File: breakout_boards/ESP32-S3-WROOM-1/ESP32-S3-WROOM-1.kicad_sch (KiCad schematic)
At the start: 47 parts, among them J1 USB_C_Receptacle_USB2.0_16P, J2 JST-XH 6 pin, J4 JST-XH 6 pin, SW1 SW_Push, SW2 SW_Push, U1 ESP32-S3-WROOM-1, U2 AP7361-33E

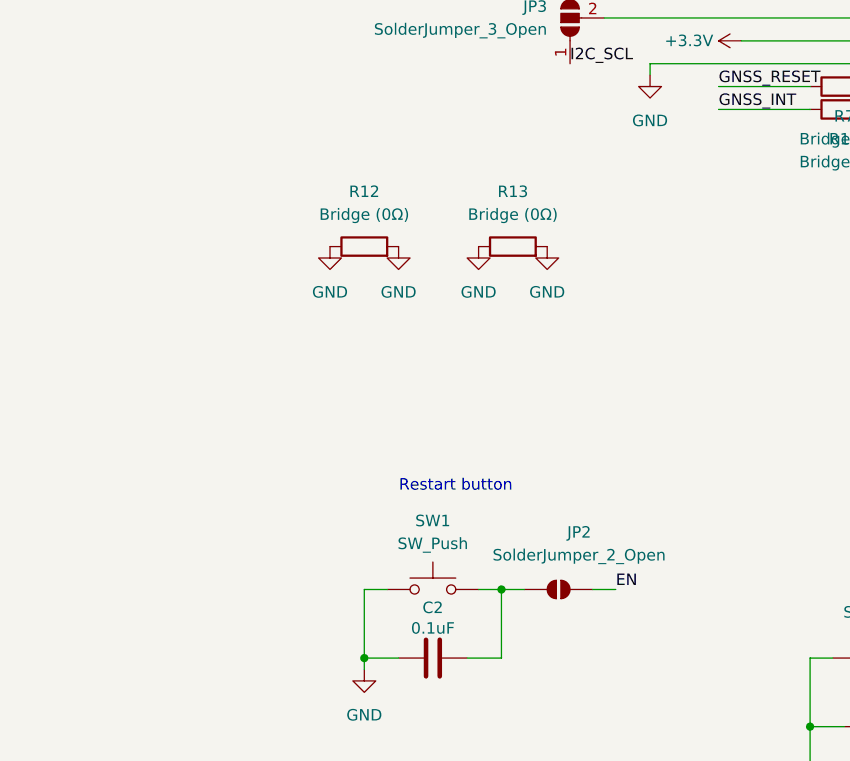
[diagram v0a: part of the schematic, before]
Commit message: Fixed ESP32-WROOM breakout board
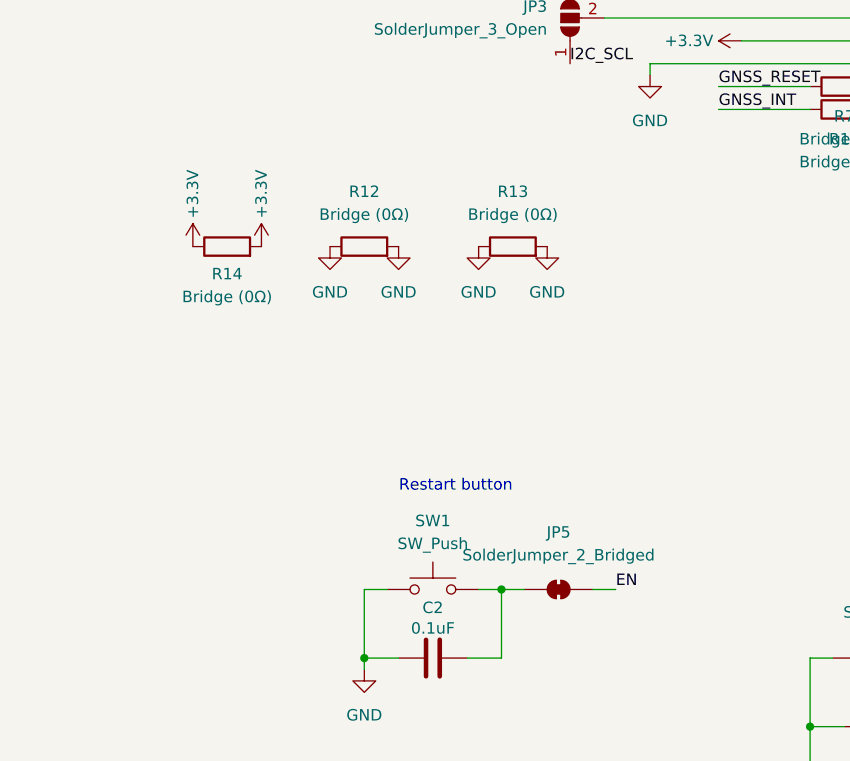
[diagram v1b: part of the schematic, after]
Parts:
- removed JP2: SolderJumper_2_Open, Jumper:SolderJumper-2_P1.3mm_Open_RoundedPad1.0x1.5mm, symbol Jumper:SolderJumper_2_Open
- added JP5: SolderJumper_2_Bridged, Jumper:SolderJumper-2_P1.3mm_Bridged_RoundedPad1.0x1.5mm, symbol Jumper:SolderJumper_2_Bridged
- added R14: Bridge (0Ω), Resistor_THT:R_Axial_DIN0207_L6.3mm_D2.5mm_P10.16mm_Horizontal, symbol Device:R
- R10: footprint Resistor_THT:R_Axial_DIN0204_L3.6mm_D1.6mm_P5.08mm_Horizontal -> Resistor_SMD:R_0603_1608Metric_Pad0.98x0.95mm_HandSolder
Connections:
- net +3.3V: now also R14.1, R14.2
- net EN: now also JP5.2 (B)
- net at C2.1, SW1.2: now also JP5.1 (A)
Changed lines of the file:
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@@
 	)
 	(symbol
+		(lib_id "Device:R")
+		(at 184.15 97.79 90)
+		(unit 1)
+		(exclude_from_sim no)
+		(in_bom yes)
+		(on_board yes)
+		(dnp no)
+		(property "Reference" "R14"
+			(at 184.15 100.838 90)
+			(effects
+				(font
+					(size 1.27 1.27)
+				)
+			)
+		)
+		(property "Value" "Bridge (0Ω)"
+			(at 184.15 103.378 90)
+			(effects
+				(font
+					(size 1.27 1.27)
+				)
+			)
+		)
+		(property "Footprint" "Resistor_THT:R_Axial_DIN0207_L6.3mm_D2.5mm_P10.16mm_Horizontal"
+			(at 184.15 99.568 90)
+			(effects
+				(font
+					(size 1.27 1.27)
+				)
+				(hide yes)
+			)
+		)
+		(property "Datasheet" "~"
+			(at 184.15 97.79 0)
+			(effects
+				(font
+					(size 1.27 1.27)
+				)
+				(hide yes)
+			)
+		)
+		(property "Description" "Resistor"
+			(at 184.15 97.79 0)
+			(effects
+				(font
+					(size 1.27 1.27)
+				)
+				(hide yes)
+			)
+		)
+		(pin "1"
+		)
+		(pin "2"
+		)
+		(instances
+			(project "ESP32-S3-WROOM-1"
+				(path "/4c0d9a6e-1f0c-494d-a3d3-03d736fc4cea"
+					(reference "R14")
+					(unit 1)
+				)
+			)
+		)
+	)
+	(symbol
 		(lib_id "Device:C")
 		(at 207.01 143.51 270)
@@
 	)
 	(symbol
+		(lib_id "power:+3.3V")
+		(at 187.96 97.79 0)
+		(unit 1)
+		(exclude_from_sim no)
+		(in_bom yes)
+		(on_board yes)
+		(dnp no)
+		(property "Reference" "#PWR035"
+			(at 187.96 101.6 0)
+			(effects
+				(font
+					(size 1.27 1.27)
+				)
+				(hide yes)
+			)
+		)
+		(property "Value" "+3.3V"
+			(at 187.96 91.948 90)
+			(effects
+				(font
+					(size 1.27 1.27)
+				)
+			)
+		)
+		(property "Footprint" ""
+			(at 187.96 97.79 0)
+			(effects
+				(font
+					(size 1.27 1.27)
+				)
+				(hide yes)
+			)
+		)
+		(property "Datasheet" ""
+			(at 187.96 97.79 0)
+			(effects
+				(font
+					(size 1.27 1.27)
+				)
+				(hide yes)
+			)
+		)
+		(property "Description" "Power symbol creates a global label with name \"+3.3V\""
+			(at 187.96 97.79 0)
+			(effects
+				(font
+					(size 1.27 1.27)
+				)
+				(hide yes)
+			)
+		)
+		(pin "1"
+		)
+		(instances
+			(project "ESP32-S3-WROOM-1"
+				(path "/4c0d9a6e-1f0c-494d-a3d3-03d736fc4cea"
+					(reference "#PWR035")
+					(unit 1)
+				)
+			)
+		)
+	)
+	(symbol
 		(lib_id "Switch:SW_Push")
 		(at 256.54 143.51 0)
@@
 	)
 	(symbol
-		(lib_id "Jumper:SolderJumper_2_Open")
-		(at 220.98 135.89 180)
-		(unit 1)
-		(exclude_from_sim no)
-		(in_bom no)
-		(on_board yes)
-		(dnp no)
-		(property "Reference" "JP2"
-			(at 223.266 129.54 0)
-			(effects
-				(font
-					(size 1.27 1.27)
-				)
-			)
-		)
-		(property "Value" "SolderJumper_2_Open"
-			(at 223.266 132.08 0)
-			(effects
-				(font
-					(size 1.27 1.27)
-				)
-			)
-		)
-		(property "Footprint" "Jumper:SolderJumper-2_P1.3mm_Open_RoundedPad1.0x1.5mm"
-			(at 220.98 135.89 0)
-			(effects
-				(font
-					(size 1.27 1.27)
-				)
-				(hide yes)
-			)
-		)
-		(property "Datasheet" "~"
-			(at 220.98 135.89 0)
-			(effects
-				(font
-					(size 1.27 1.27)
-				)
-				(hide yes)
-			)
-		)
-		(property "Description" "Solder Jumper, 2-pole, open"
-			(at 220.98 135.89 0)
-			(effects
-				(font
-					(size 1.27 1.27)
-				)
-				(hide yes)
-			)
-		)
-		(pin "1"
-		)
-		(pin "2"
-		)
-		(instances
-			(project "ESP32-S3-WROOM-1"
-				(path "/4c0d9a6e-1f0c-494d-a3d3-03d736fc4cea"
-					(reference "JP2")
-					(unit 1)
-				)
-			)
-		)
-	)
-	(symbol
 		(lib_id "Device:C")
 		(at 78.74 59.69 0)
@@
 			)
 		)
-		(property "Footprint" "Resistor_THT:R_Axial_DIN0204_L3.6mm_D1.6mm_P5.08mm_Horizontal"
+		(property "Footprint" "Resistor_SMD:R_0603_1608Metric_Pad0.98x0.95mm_HandSolder"
 			(at 263.652 137.16 90)
 			(effects
@@
 	)
 	(symbol
+		(lib_id "power:+3.3V")
+		(at 180.34 97.79 0)
+		(unit 1)
+		(exclude_from_sim no)
+		(in_bom yes)
+		(on_board yes)
+		(dnp no)
+		(property "Reference" "#PWR033"
+			(at 180.34 101.6 0)
+			(effects
+				(font
+					(size 1.27 1.27)
+				)
+				(hide yes)
+			)
+		)
+		(property "Value" "+3.3V"
+			(at 180.34 91.948 90)
+			(effects
+				(font
+					(size 1.27 1.27)
+				)
+			)
+		)
+		(property "Footprint" ""
+			(at 180.34 97.79 0)
+			(effects
+				(font
+					(size 1.27 1.27)
+				)
+				(hide yes)
+			)
+		)
+		(property "Datasheet" ""
+			(at 180.34 97.79 0)
+			(effects
+				(font
+					(size 1.27 1.27)
+				)
+				(hide yes)
+			)
+		)
+		(property "Description" "Power symbol creates a global label with name \"+3.3V\""
+			(at 180.34 97.79 0)
+			(effects
+				(font
+					(size 1.27 1.27)
+				)
+				(hide yes)
+			)
+		)
+		(pin "1"
+		)
+		(instances
+			(project "ESP32-S3-WROOM-1"
+				(path "/4c0d9a6e-1f0c-494d-a3d3-03d736fc4cea"
+					(reference "#PWR033")
+					(unit 1)
+				)
+			)
+		)
+	)
+	(symbol
 		(lib_id "Connector_Generic:Conn_01x06")
 		(at 261.62 38.1 0)
@@
 					(unit 1)
 				)
+			)
+		)
+	)
+	(symbol
+		(lib_id "Jumper:SolderJumper_2_Bridged")
+		(at 220.98 135.89 0)
+		(unit 1)
+		(exclude_from_sim no)
+		(in_bom no)
+		(on_board yes)
+		(dnp no)
+		(fields_autoplaced yes)
+		(property "Reference" "JP5"
+			(at 220.98 129.54 0)
+			(effects
+				(font
+					(size 1.27 1.27)
+				)
+			)
+		)
+		(property "Value" "SolderJumper_2_Bridged"
+			(at 220.98 132.08 0)
+			(effects
+				(font
+					(size 1.27 1.27)
+				)
+			)
+		)
+		(property "Footprint" "Jumper:SolderJumper-2_P1.3mm_Bridged_RoundedPad1.0x1.5mm"
+			(at 220.98 135.89 0)
+			(effects
+				(font
+					(size 1.27 1.27)
+				)
+				(hide yes)
+			)
+		)
+		(property "Datasheet" "~"
+			(at 220.98 135.89 0)
+			(effects
+				(font
+					(size 1.27 1.27)
+				)
+				(hide yes)
+			)
+		)
+		(property "Description" "Solder Jumper, 2-pole, closed/bridged"
+			(at 220.98 135.89 0)
+			(effects
+				(font
+					(size 1.27 1.27)
+				)
+				(hide yes)
+			)
+		)
+		(pin "2"
+		)
+		(pin "1"
+		)
+		(instances
+			(project ""
+				(path "/4c0d9a6e-1f0c-494d-a3d3-03d736fc4cea"
+					(reference "JP5")
+					(unit 1)
+				)

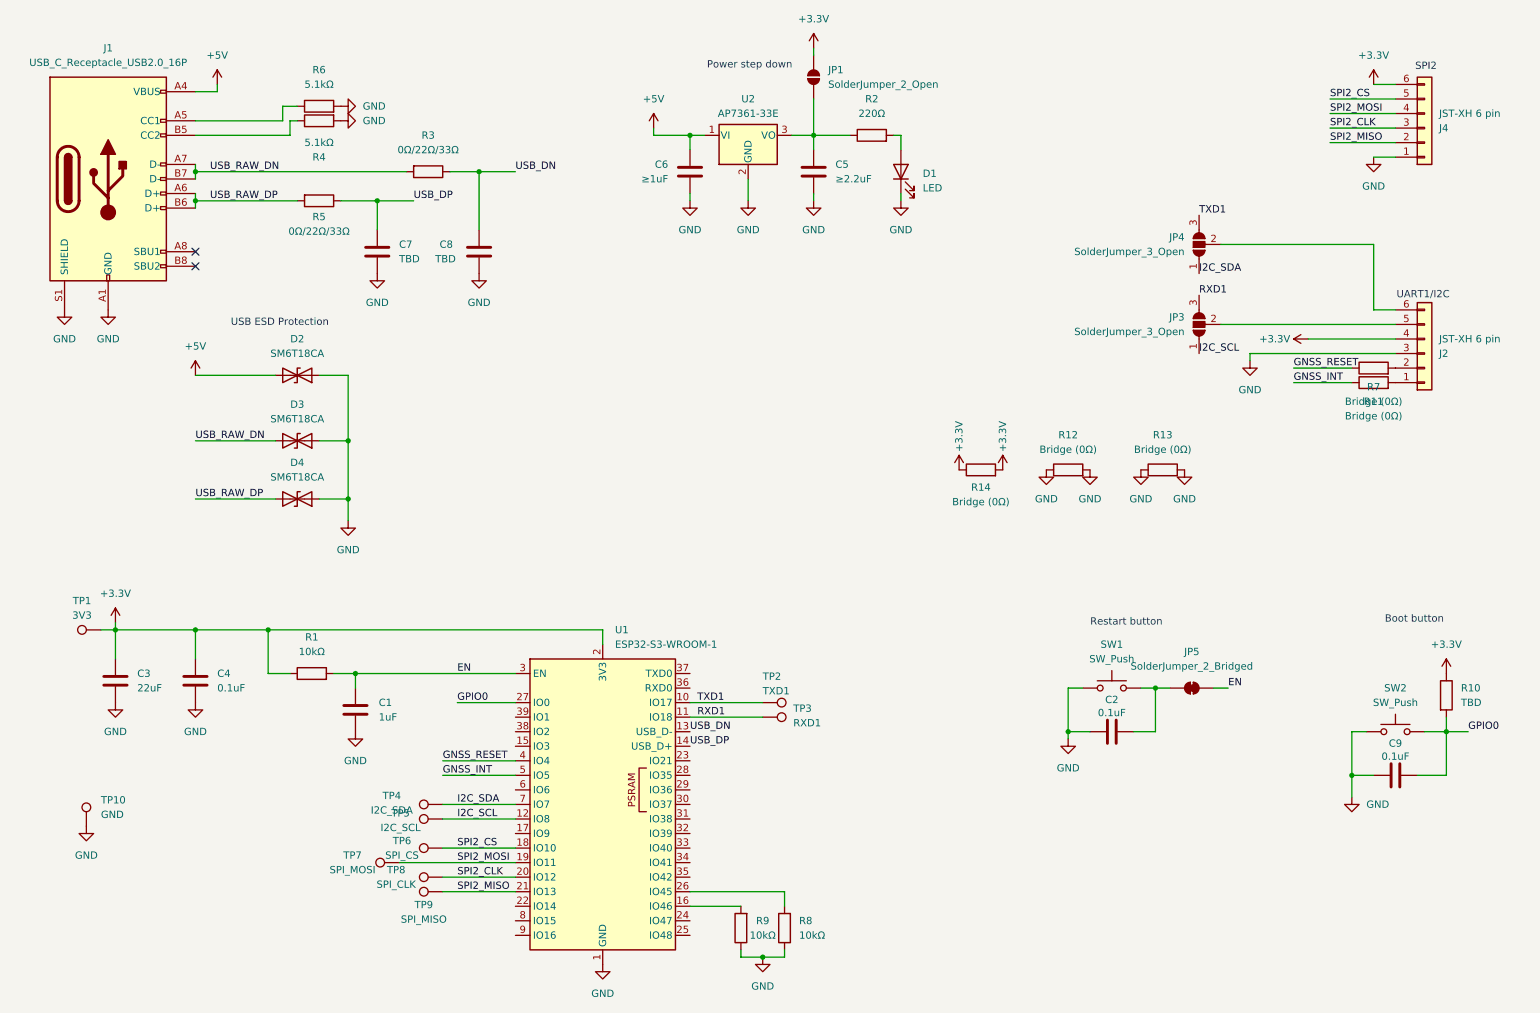
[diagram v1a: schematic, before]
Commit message: edited values to match real life and added text
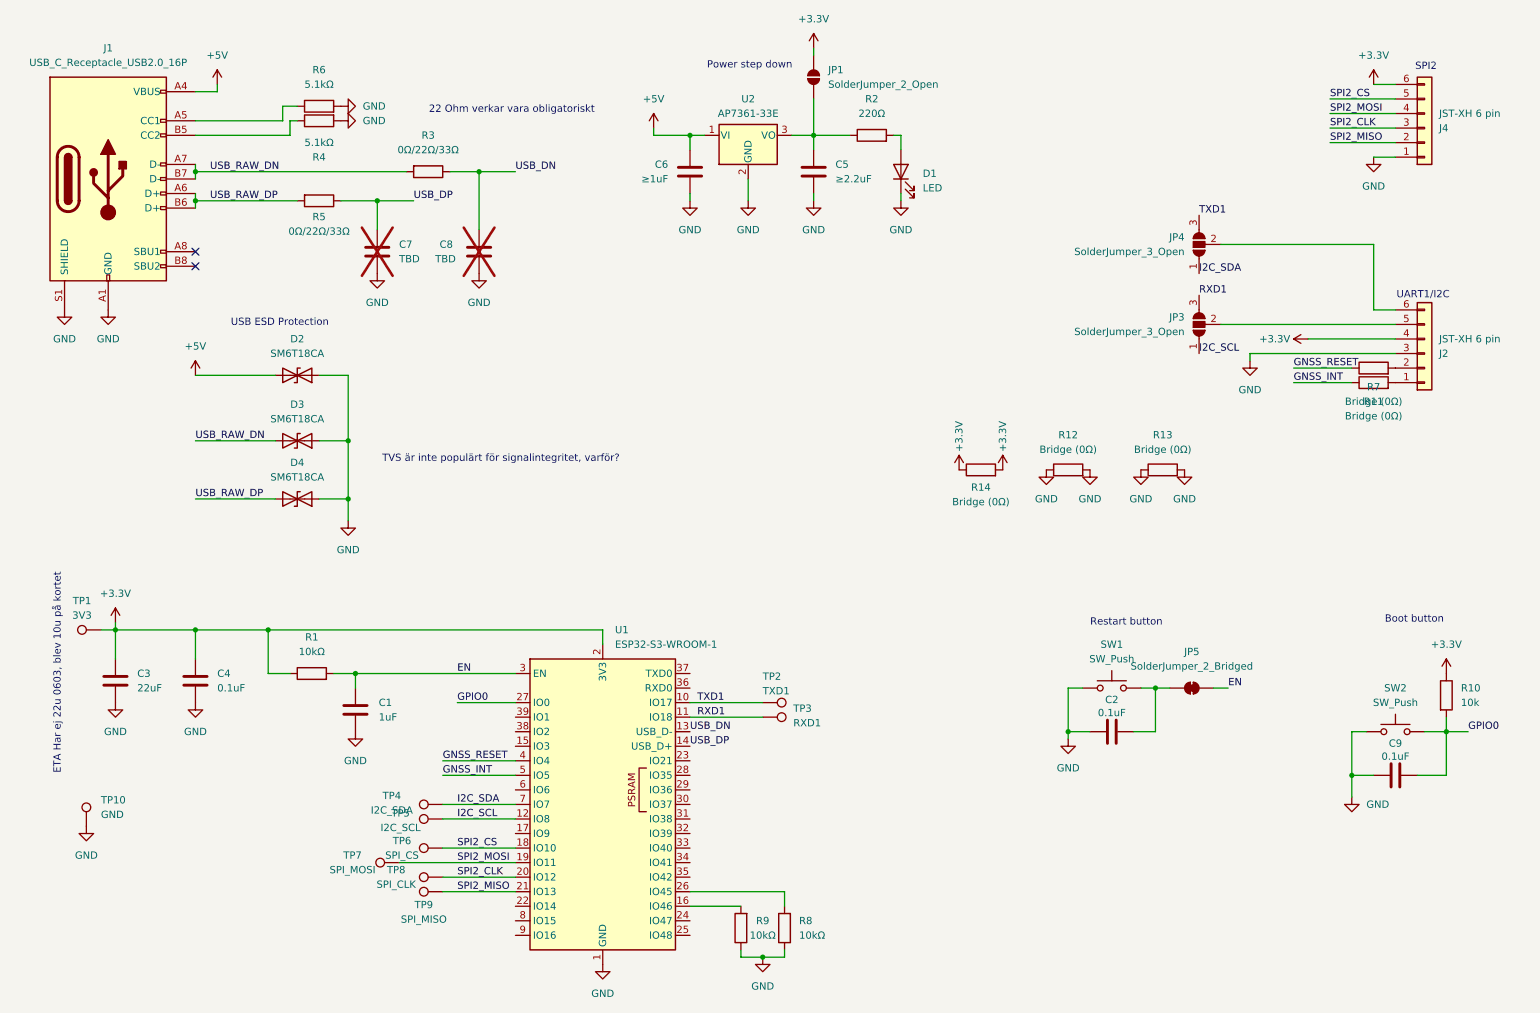
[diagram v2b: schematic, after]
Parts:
- C7, C8: now not fitted
- R10: value TBD -> 10k
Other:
- note added: "22 Ohm verkar vara obligatoriskt"
- note added: "ETA Har ej 22u 0603, blev 10u på kortet"
- note added: "TVS är inte populärt för signalintegritet, varför?"

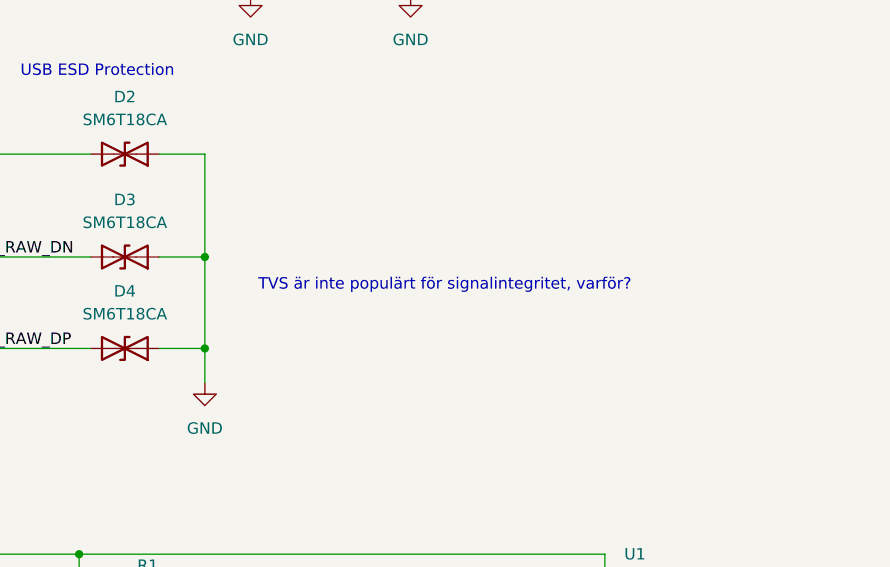
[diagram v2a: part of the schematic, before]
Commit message: fixed some ERC errors and warnings, added USB, assigned a bunch of footprints
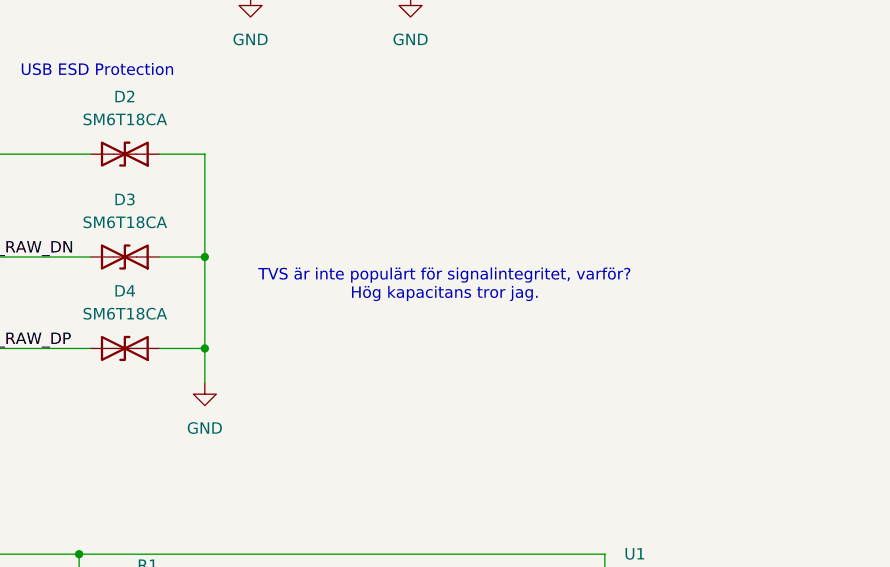
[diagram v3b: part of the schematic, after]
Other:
- note added: "TVS är inte populärt för signalintegritet, varför? Hög kapacitans tror jag."
- note removed: "TVS är inte populärt för signalintegritet, varför?"
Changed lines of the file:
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@@
 		)
 	)
-	(text "TVS är inte populärt för signalintegritet, varför?"
+	(text "TVS är inte populärt för signalintegritet, varför?\nHög kapacitans tror jag."
 		(exclude_from_sim no)
 		(at 100.33 95.885 0)
